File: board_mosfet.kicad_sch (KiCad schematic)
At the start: 4 parts, among them J2 USB_IN, U1 AMS1117-3.3

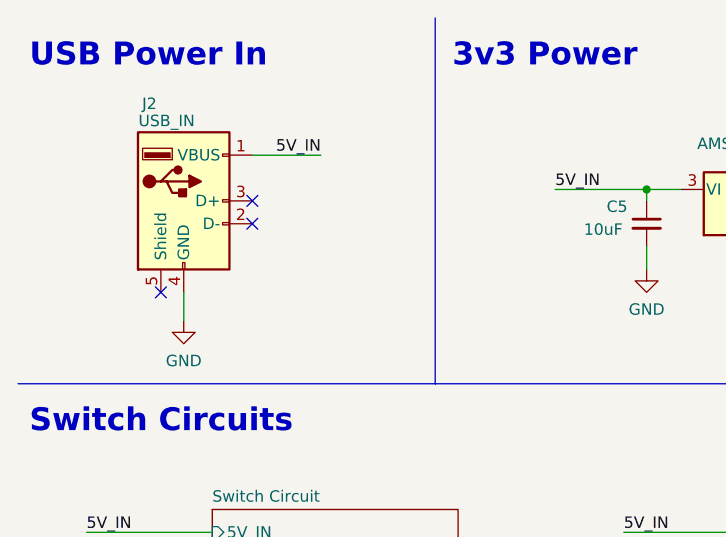
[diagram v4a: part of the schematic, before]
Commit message: Added resistor between D+ and D-
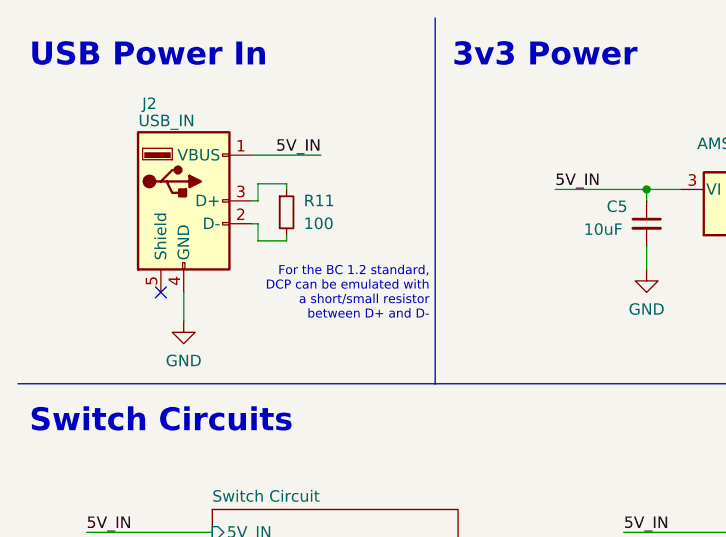
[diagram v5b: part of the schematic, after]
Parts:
- added R11: 100, Resistor_SMD:R_0603_1608Metric, symbol Device:R_Small
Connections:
- net at J2.2 (D-): now also R11.2
- net at J2.3 (D+): now also R11.1
- no-connect marks 3 -> 1
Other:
- note added: "For the BC 1.2 standard, DCP can be emulated with a short/small resistor between D+ and D-"
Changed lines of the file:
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@@
     (title "Wifi USB Port")
     (date "2023-02-05")
-    (rev "0.2.0")
+    (rev "0.2.1")
   )
   (junction (at 65.405 90.17) (diameter 0) (color 0 0 0 0)
@@
   (junction (at 105.41 31.115) (diameter 0) (color 0 0 0 0)
   )
-  (no_connect (at 38.1 32.385))
-  (no_connect (at 38.1 34.925))
   (no_connect (at 27.94 42.545))
   (polyline (pts (xy 128.27 12.065) (xy 128.27 52.705))
     (stroke (width 0) (type default) (color 0 0 0 0))
   )
+  (wire (pts (xy 38.1 34.925) (xy 38.735 34.925))
+    (stroke (width 0) (type default) (color 0 0 0 0))
+  )
   (polyline (pts (xy 58.42 12.065) (xy 58.42 52.705))
     (stroke (width 0) (type default) (color 0 0 0 0))
   )
+  (wire (pts (xy 41.91 36.195) (xy 41.91 36.83))
+    (stroke (width 0) (type default) (color 0 0 0 0))
+  )
   (wire (pts (xy 147.32 27.94) (xy 158.75 27.94))
     (stroke (width 0) (type default) (color 0 0 0 0))
@@
     (stroke (width 0) (type default) (color 0 0 0 0))
   )
+  (wire (pts (xy 41.91 30.48) (xy 41.91 31.115))
+    (stroke (width 0) (type default) (color 0 0 0 0))
+  )
   (wire (pts (xy 158.75 43.18) (xy 147.32 43.18))
     (stroke (width 0) (type default) (color 0 0 0 0))
   )
+  (wire (pts (xy 38.1 32.385) (xy 38.735 32.385))
+    (stroke (width 0) (type default) (color 0 0 0 0))
+  )
   (wire (pts (xy 176.53 38.1) (xy 173.355 38.1))
     (stroke (width 0) (type default) (color 0 0 0 0))
@@
     (stroke (width 0) (type default) (color 0 0 0 0))
   )
+  (wire (pts (xy 38.735 32.385) (xy 38.735 30.48))
+    (stroke (width 0) (type default) (color 0 0 0 0))
+  )
   (wire (pts (xy 38.1 27.305) (xy 45.72 27.305))
     (stroke (width 0) (type default) (color 0 0 0 0))
@@
     (stroke (width 0) (type default) (color 0 0 0 0))
   )
+  (wire (pts (xy 38.735 34.925) (xy 38.735 36.83))
+    (stroke (width 0) (type default) (color 0 0 0 0))
+  )
   (wire (pts (xy 81.915 31.115) (xy 81.915 32.385))
     (stroke (width 0) (type default) (color 0 0 0 0))
@@
     (stroke (width 0) (type default) (color 0 0 0 0))
   )
+  (wire (pts (xy 38.735 30.48) (xy 41.91 30.48))
+    (stroke (width 0) (type default) (color 0 0 0 0))
+  )
   (wire (pts (xy 105.41 31.115) (xy 105.41 32.385))
     (stroke (width 0) (type default) (color 0 0 0 0))
@@
   )
   (wire (pts (xy 120.65 86.995) (xy 130.175 86.995))
+    (stroke (width 0) (type default) (color 0 0 0 0))
+  )
+  (wire (pts (xy 38.735 36.83) (xy 41.91 36.83))
     (stroke (width 0) (type default) (color 0 0 0 0))
   )
@@
   (text "BIDIR" (at 170.815 34.925 0)
     (effects (font (size 1.27 1.27) (thickness 0.254) bold) (justify left bottom))
+  )
+  (text "For the BC 1.2 standard,\nDCP can be emulated with\na short/small resistor\nbetween D+ and D-\n"
+    (at 57.785 45.72 0)
+    (effects (font (size 1 1)) (justify right bottom))
   )
   (text "Switch Circuits" (at 13.335 58.42 0)
@@
       (effects (font (size 1.27 1.27)) hide)
     )
+    (pin "1")
+    (pin "2")
+  )
+  (symbol (lib_id "Device:R_Small") (at 41.91 33.655 0) (unit 1)
+    (in_bom yes) (on_board yes)
+    (property "Reference" "R11" (id 0) (at 43.815 32.3849 0)
+      (effects (font (size 1.27 1.27)) (justify left))
+    )
+    (property "Value" "100" (id 1) (at 43.815 34.9249 0)
+      (effects (font (size 1.27 1.27)) (justify left))
+    )
+    (property "Footprint" "Resistor_SMD:R_0603_1608Metric" (id 2) (at 41.91 33.655 0)
+      (effects (font (size 1.27 1.27)) hide)
+    )
+    (property "Datasheet" "~" (id 3) (at 41.91 33.655 0)
+      (effects (font (size 1.27 1.27)) hide)
+    )
+    (property "LCSC Part Number" "C22775" (id 4) (at 41.91 33.655 0)
+      (effects (font (size 1.27 1.27)) hide)
+    )
+    (property "Manufacturer" "UNI-ROYAL(Uniroyal Elec)" (id 5) (at 41.91 33.655 0)
+      (effects (font (size 1.27 1.27)) hide)
+    )
+    (property "Manufacturer Part Number" "0603WAF1000T5E" (id 6) (at 41.91 33.655 0)
+      (effects (font (size 1.27 1.27)) hide)
+    )
